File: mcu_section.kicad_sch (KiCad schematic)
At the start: 1 part, among them U1 ESP32-D0WDQ6

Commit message: viper22as, transformer, hierarchical connections
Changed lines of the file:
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@@
 (kicad_sch (version 20230121) (generator eeschema)
   (paper "A4")
+  (hierarchical_label "Gnd in" (shape input) (at 144.78 38.1 0) (fields_autoplaced)
+    (effects (font (size 1.27 1.27)) (justify left))
+  )
+  (hierarchical_label "TRIAC output" (shape output) (at 144.78 43.18 0) (fields_autoplaced)
+    (effects (font (size 1.27 1.27)) (justify left))
+  )
+  (hierarchical_label "3.3V in" (shape input) (at 144.78 33.02 0) (fields_autoplaced)
+    (effects (font (size 1.27 1.27)) (justify left))
+  )
+  (hierarchical_label "ZV signal in" (shape input) (at 144.78 48.26 0) (fields_autoplaced)
+    (effects (font (size 1.27 1.27)) (justify left))
+  )
   (symbol (lib_id "2023-07-31_14-21-16:ESP32-D0WDQ6") (at 165.1 78.74 0) (unit 2)
     (in_bom yes) (on_board yes) (dnp no) (fields_autoplaced)

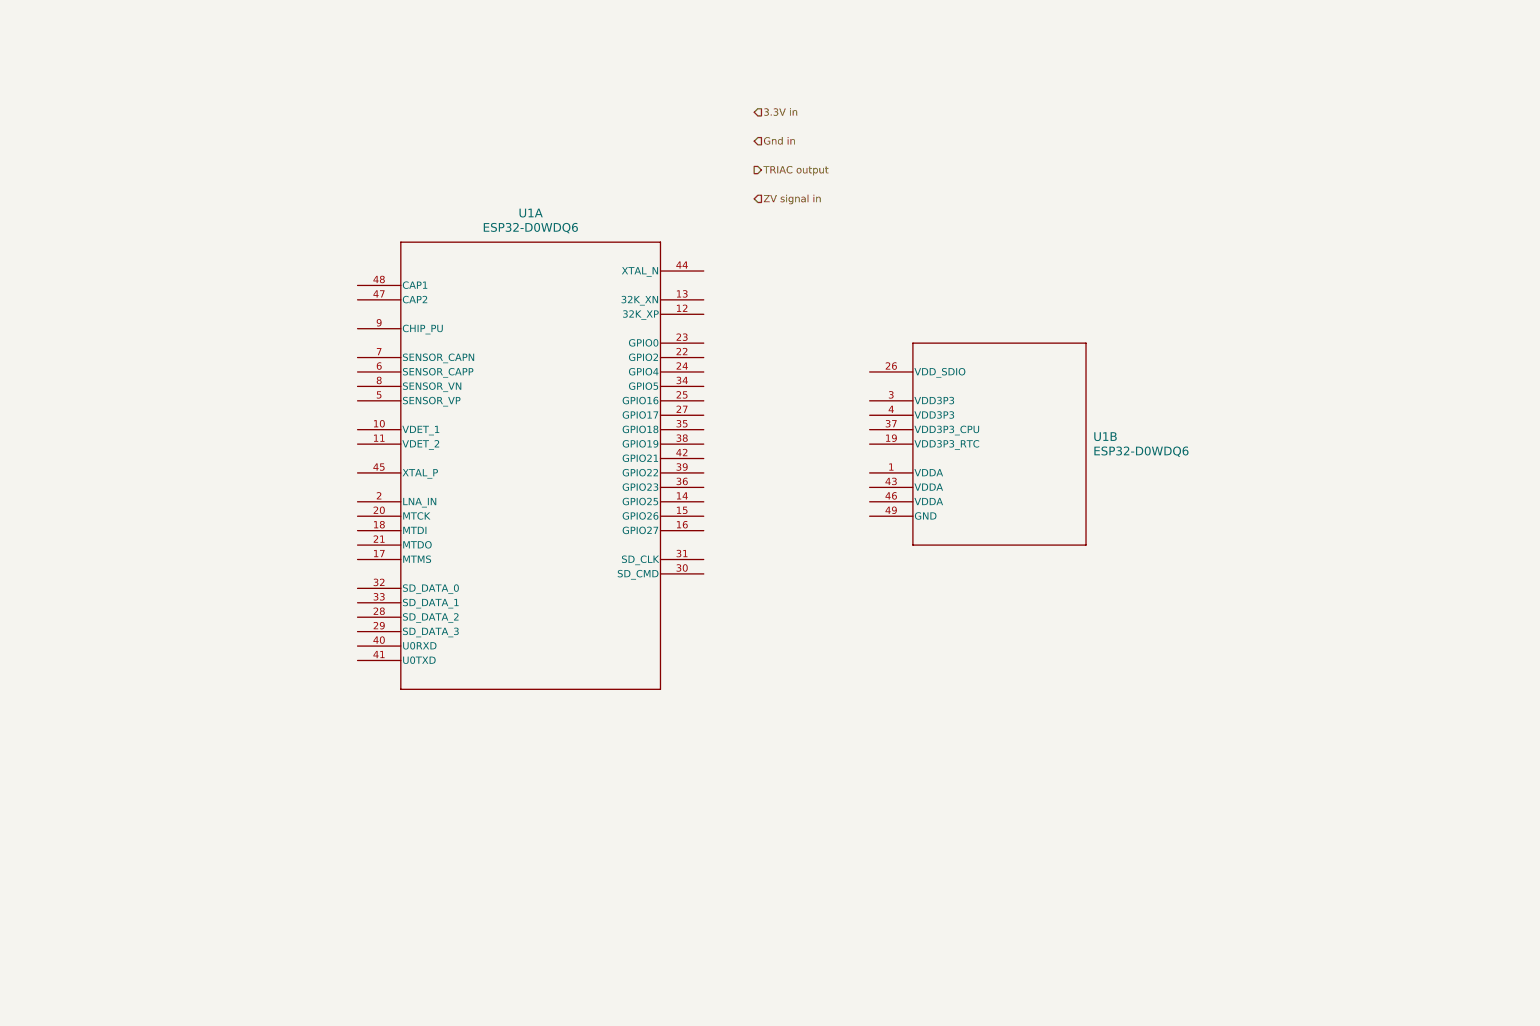
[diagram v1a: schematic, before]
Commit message: completed psu schematic sheet
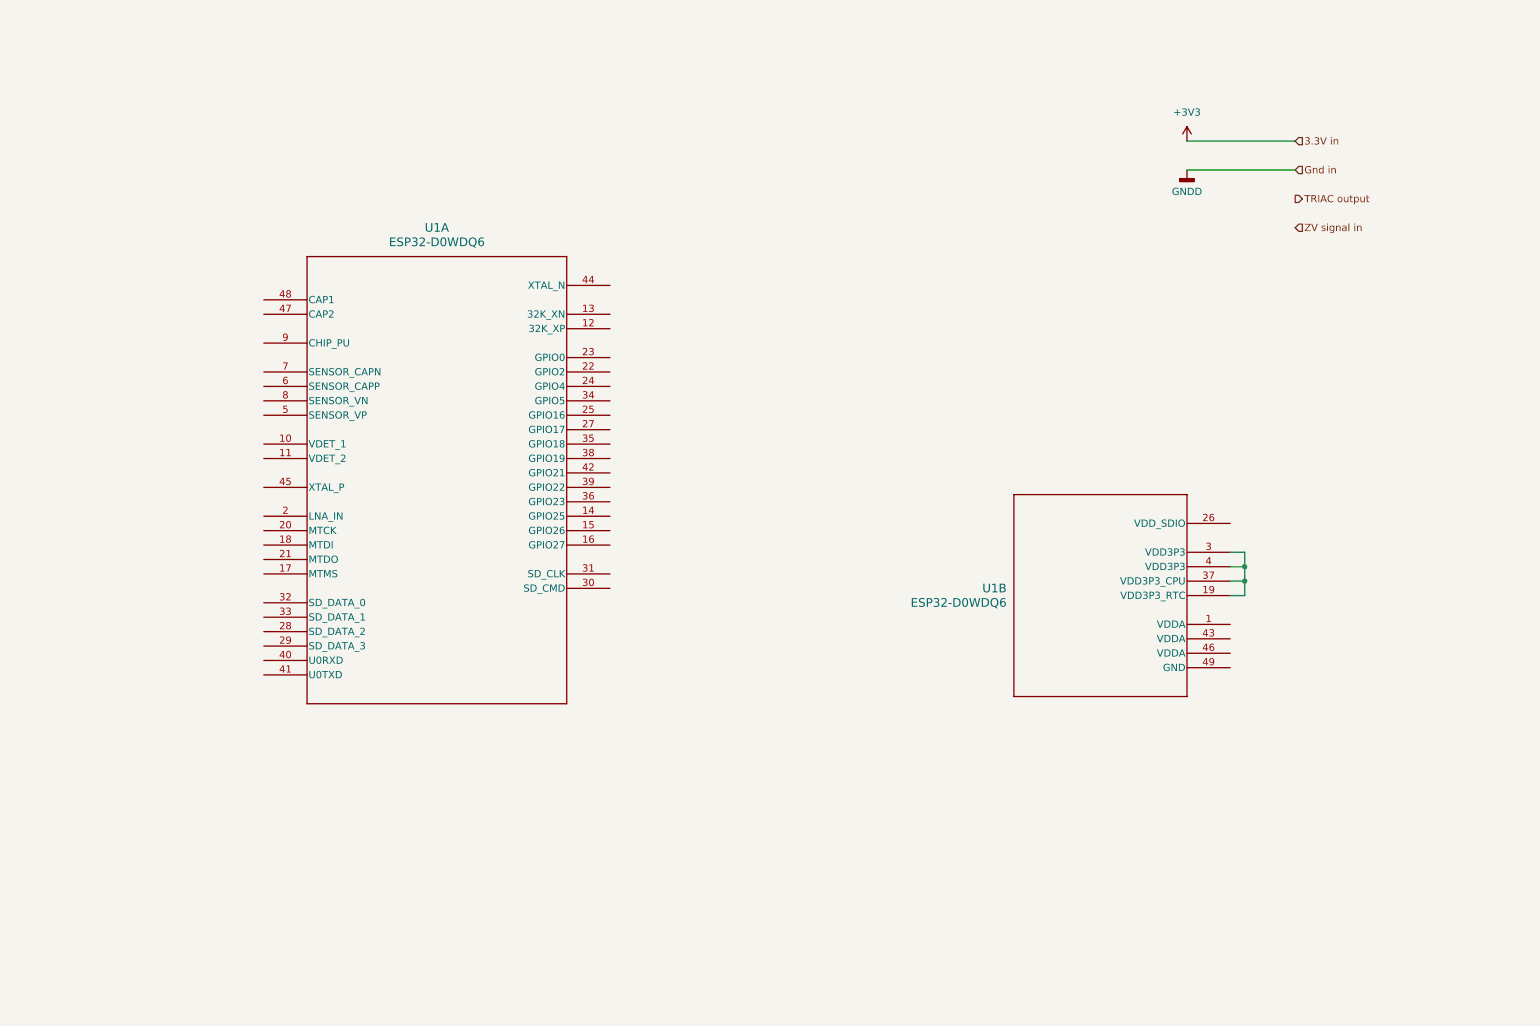
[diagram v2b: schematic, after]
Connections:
- net at U1.19 (VDD3P3_RTC): now also U1.3 (VDD3P3), U1.37 (VDD3P3_CPU), U1.4 (VDD3P3)
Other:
- moved on the sheet: U1A, U1B
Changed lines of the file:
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@@
 (kicad_sch (version 20230121) (generator eeschema)
   (paper "A4")
-  (hierarchical_label "Gnd in" (shape input) (at 144.78 38.1 0) (fields_autoplaced)
+  (junction (at 231.14 115.57) (diameter 0) (color 0 0 0 0)
+  )
+  (junction (at 231.14 113.03) (diameter 0) (color 0 0 0 0)
+  )
+  (wire (pts (xy 231.14 115.57) (xy 231.14 118.11))
+    (stroke (width 0) (type default))
+  )
+  (wire (pts (xy 231.14 113.03) (xy 231.14 115.57))
+    (stroke (width 0) (type default))
+  )
+  (wire (pts (xy 231.14 113.03) (xy 228.6 113.03))
+    (stroke (width 0) (type default))
+  )
+  (wire (pts (xy 231.14 118.11) (xy 228.6 118.11))
+    (stroke (width 0) (type default))
+  )
+  (wire (pts (xy 228.6 110.49) (xy 231.14 110.49))
+    (stroke (width 0) (type default))
+  )
+  (wire (pts (xy 220.98 43.18) (xy 240.03 43.18))
+    (stroke (width 0) (type default))
+  )
+  (wire (pts (xy 220.98 38.1) (xy 240.03 38.1))
+    (stroke (width 0) (type default))
+  )
+  (wire (pts (xy 231.14 115.57) (xy 228.6 115.57))
+    (stroke (width 0) (type default))
+  )
+  (wire (pts (xy 231.14 110.49) (xy 231.14 113.03))
+    (stroke (width 0) (type default))
+  )
+  (hierarchical_label "Gnd in" (shape input) (at 240.03 43.18 0) (fields_autoplaced)
     (effects (font (size 1.27 1.27)) (justify left))
   )
-  (hierarchical_label "TRIAC output" (shape output) (at 144.78 43.18 0) (fields_autoplaced)
+  (hierarchical_label "TRIAC output" (shape output) (at 240.03 48.26 0) (fields_autoplaced)
     (effects (font (size 1.27 1.27)) (justify left))
   )
-  (hierarchical_label "3.3V in" (shape input) (at 144.78 33.02 0) (fields_autoplaced)
+  (hierarchical_label "3.3V in" (shape input) (at 240.03 38.1 0) (fields_autoplaced)
     (effects (font (size 1.27 1.27)) (justify left))
   )
-  (hierarchical_label "ZV signal in" (shape input) (at 144.78 48.26 0) (fields_autoplaced)
+  (hierarchical_label "ZV signal in" (shape input) (at 240.03 53.34 0) (fields_autoplaced)
     (effects (font (size 1.27 1.27)) (justify left))
   )
-  (symbol (lib_id "2023-07-31_14-21-16:ESP32-D0WDQ6") (at 165.1 78.74 0) (unit 2)
+  (symbol (lib_id "power:+3V3") (at 220.98 38.1 0) (unit 1)
     (in_bom yes) (on_board yes) (dnp no) (fields_autoplaced)
-    (property "Reference" "U1" (at 204.47 90.17 0)
+    (property "Reference" "#PWR05" (at 220.98 41.91 0)
+      (effects (font (size 1.27 1.27)) hide)
+    )
+    (property "Value" "+3V3" (at 220.98 33.02 0)
+      (effects (font (size 1.27 1.27)))
+    )
+    (property "Footprint" "" (at 220.98 38.1 0)
+      (effects (font (size 1.27 1.27)) hide)
+    )
+    (property "Datasheet" "" (at 220.98 38.1 0)
+      (effects (font (size 1.27 1.27)) hide)
+    )
+    (pin "1")
+    (instances
+      (project "esp32-iot-socket"
+        (path "/45e1e5e5-a388-432c-8d2b-80b7f8345075/1dc68658-e7d3-43ab-9cff-123756104291"
+          (reference "#PWR05") (unit 1)
+        )
+      )
+    )
+  )
+  (symbol (lib_id "power:GNDD") (at 220.98 43.18 0) (unit 1)
+    (in_bom yes) (on_board yes) (dnp no) (fields_autoplaced)
+    (property "Reference" "#PWR04" (at 220.98 49.53 0)
+      (effects (font (size 1.27 1.27)) hide)
+    )
+    (property "Value" "GNDD" (at 220.98 46.99 0)
+      (effects (font (size 1.27 1.27)))
+    )
+    (property "Footprint" "" (at 220.98 43.18 0)
+      (effects (font (size 1.27 1.27)) hide)
+    )
+    (property "Datasheet" "" (at 220.98 43.18 0)
+      (effects (font (size 1.27 1.27)) hide)
+    )
+    (pin "1")
+    (instances
+      (project "esp32-iot-socket"
+        (path "/45e1e5e5-a388-432c-8d2b-80b7f8345075/1dc68658-e7d3-43ab-9cff-123756104291"
+          (reference "#PWR04") (unit 1)
+        )
+      )
+    )
+  )
+  (symbol (lib_id "2023-07-31_14-21-16:ESP32-D0WDQ6") (at 228.6 105.41 0) (mirror y) (unit 2)
+    (in_bom yes) (on_board yes) (dnp no)
+    (property "Reference" "U1" (at 189.23 116.84 0)
       (effects (font (size 1.524 1.524)) (justify left))
     )
-    (property "Value" "ESP32-D0WDQ6" (at 204.47 92.71 0)
+    (property "Value" "ESP32-D0WDQ6" (at 189.23 119.38 0)
       (effects (font (size 1.524 1.524)) (justify left))
     )
-    (property "Footprint" "Package_DFN_QFN:QFN-48-1EP_6x6mm_P0.4mm_EP4.3x4.3mm_ThermalVias" (at 165.1 78.74 0)
+    (property "Footprint" "Package_DFN_QFN:QFN-48-1EP_6x6mm_P0.4mm_EP4.3x4.3mm_ThermalVias" (at 228.6 105.41 0)
       (effects (font (size 1.27 1.27) italic) hide)
     )
-    (property "Datasheet" "ESP32-D0WDQ6" (at 165.1 78.74 0)
+    (property "Datasheet" "ESP32-D0WDQ6" (at 228.6 105.41 0)
       (effects (font (size 1.27 1.27) italic) hide)
     )
@@
     )
   )
-  (symbol (lib_id "2023-07-31_14-21-16:ESP32-D0WDQ6") (at 74.93 63.5 0) (unit 1)
+  (symbol (lib_id "2023-07-31_14-21-16:ESP32-D0WDQ6") (at 58.42 66.04 0) (unit 1)
     (in_bom yes) (on_board yes) (dnp no) (fields_autoplaced)
-    (property "Reference" "U1" (at 105.41 50.8 0)
+    (property "Reference" "U1" (at 88.9 53.34 0)
       (effects (font (size 1.524 1.524)))
     )
-    (property "Value" "ESP32-D0WDQ6" (at 105.41 53.34 0)
+    (property "Value" "ESP32-D0WDQ6" (at 88.9 55.88 0)
       (effects (font (size 1.524 1.524)))
     )
-    (property "Footprint" "Package_DFN_QFN:QFN-48-1EP_6x6mm_P0.4mm_EP4.3x4.3mm_ThermalVias" (at 74.93 63.5 0)
+    (property "Footprint" "Package_DFN_QFN:QFN-48-1EP_6x6mm_P0.4mm_EP4.3x4.3mm_ThermalVias" (at 58.42 66.04 0)
       (effects (font (size 1.27 1.27) italic) hide)
     )
-    (property "Datasheet" "ESP32-D0WDQ6" (at 74.93 63.5 0)
+    (property "Datasheet" "ESP32-D0WDQ6" (at 58.42 66.04 0)
       (effects (font (size 1.27 1.27) italic) hide)
     )

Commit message: added buttons, crystal, power caps
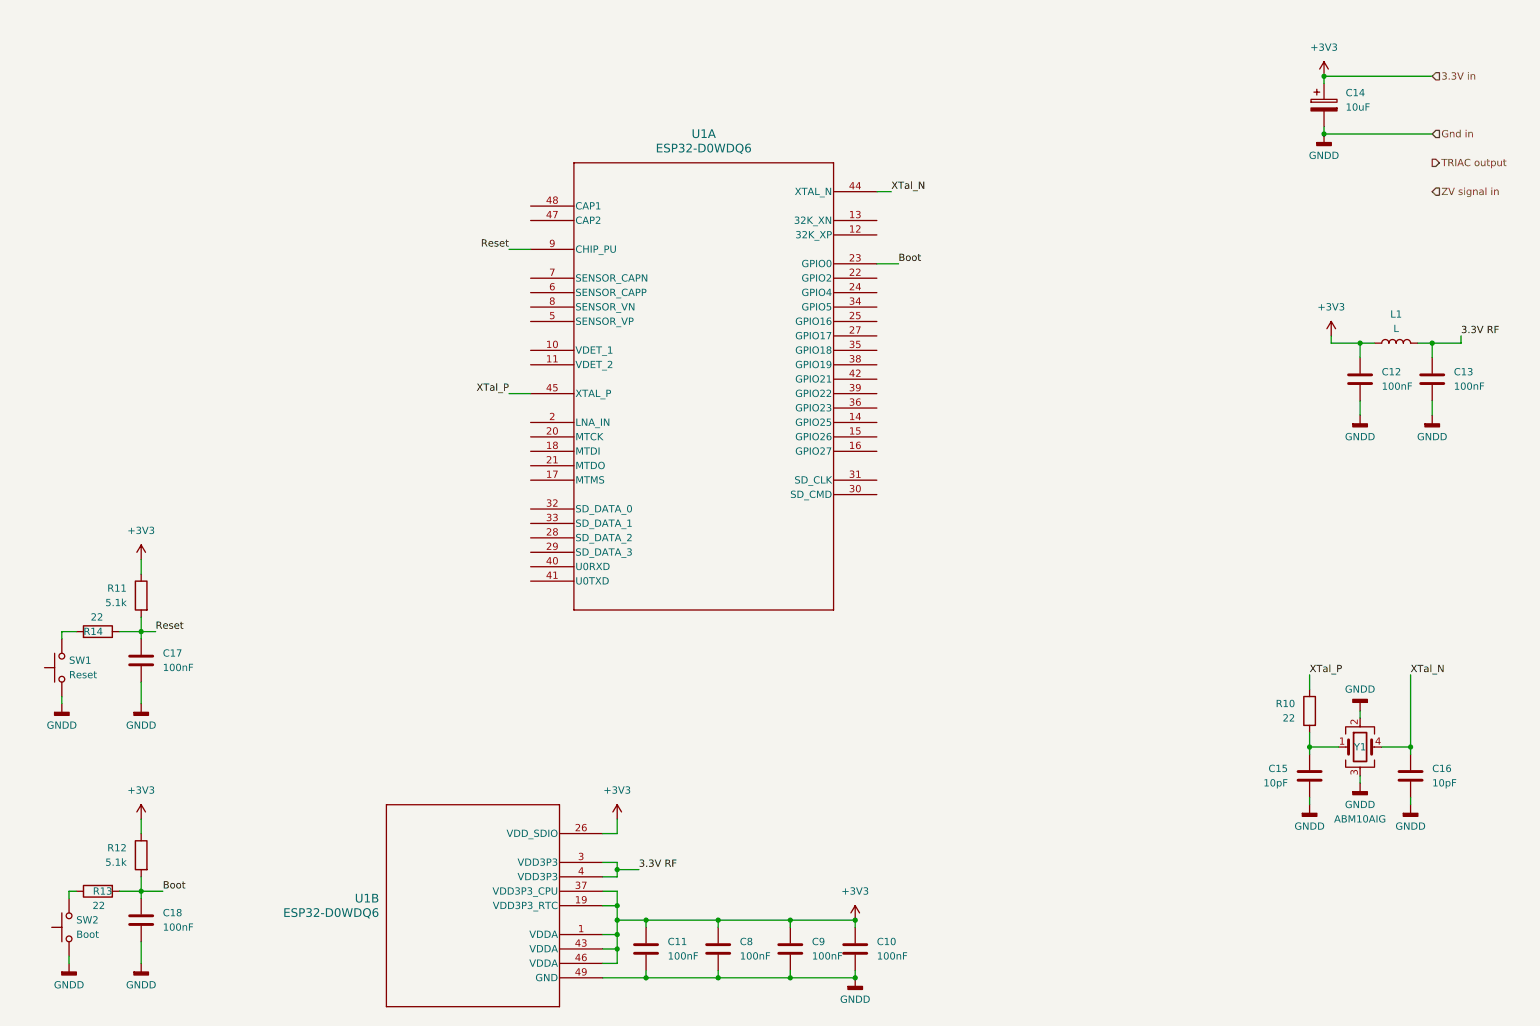
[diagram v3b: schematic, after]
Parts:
- added C10, C11, C12, C13, C17, C18, C8, C9: 100nF, Capacitor_SMD:C_1206_3216Metric, symbol Device:C
- added C14: 10uF, Capacitor_Tantalum_SMD:CP_EIA-6032-20_AVX-F_Pad2.25x2.35mm_HandSolder, symbol Device:C_Polarized
- added C15, C16: 10pF, Capacitor_SMD:C_0603_1608Metric_Pad1.08x0.95mm_HandSolder, symbol Device:C
- added L1: L, symbol Device:L
- added R10, R13, R14: 22, Resistor_SMD:R_0603_1608Metric_Pad0.98x0.95mm_HandSolder, symbol Device:R
- added R11, R12: 5.1k, Resistor_SMD:R_0603_1608Metric_Pad0.98x0.95mm_HandSolder, symbol Device:R
- added SW1: Reset, Button_Switch_SMD:SW_SPST_B3U-1000P-B, symbol Switch:SW_Push
- added SW2: Boot, Button_Switch_SMD:SW_SPST_B3U-1000P-B, symbol Switch:SW_Push
- added Y1: ABM10AIG, Oscillator:Oscillator_SMD_Abracon_ASDMB-4Pin_2.5x2.0mm, symbol Device:Crystal_GND23
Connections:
- net +3V3: now also U1.1 (VDDA), U1.19 (VDD3P3_RTC), U1.26 (VDD_SDIO), U1.37 (VDD3P3_CPU), U1.43 (VDDA), U1.46 (VDDA), C10.1, C11.1, C12.1, C14.1, C8.1, C9.1, L1.1, R11.1, R12.1
- net GNDD: now also U1.49 (GND), C10.2, C11.2, C12.2, C13.2, C14.2, C15.2, C16.2, C17.2, C18.2, C8.2, C9.2, SW1.1, SW2.1, Y1.2, Y1.3
- net 3.3V RF: now reaches U1.3 (VDD3P3), U1.4 (VDD3P3)
- net 3.3V RF: now also C13.1, L1.2; no longer U1.19 (VDD3P3_RTC), U1.37 (VDD3P3_CPU)
- net Boot: now reaches U1.23 (GPIO0)
- net Boot: now also C18.1, R12.2, R13.2
- net XTal_N: now reaches U1.44 (XTAL_N)
- net XTal_N: now also C16.1, Y1.4
- net XTal_P: now reaches U1.45 (XTAL_P)
- net XTal_P: now also R10.1
- net Reset: now reaches U1.9 (CHIP_PU)
- net Reset: now also C17.1, R11.2, R14.1
- new net: C15.1, R10.2, Y1.1
- new net: R14.2, SW1.2
- new net: R13.1, SW2.2
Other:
- moved on the sheet: U1A, U1B
